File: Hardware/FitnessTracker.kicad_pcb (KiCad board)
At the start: 2 copper layers, 16.6 x 16.7 mm, 8 parts, among them IC1 MAX30102, Q1 BSS138, Q2 BSS138, Q3 BSS138, U1 STM32WB15CCU6E, U2 LIS2DS12TR, U3 MS560702BA03-50, U4 ublox_SAM-M8Q

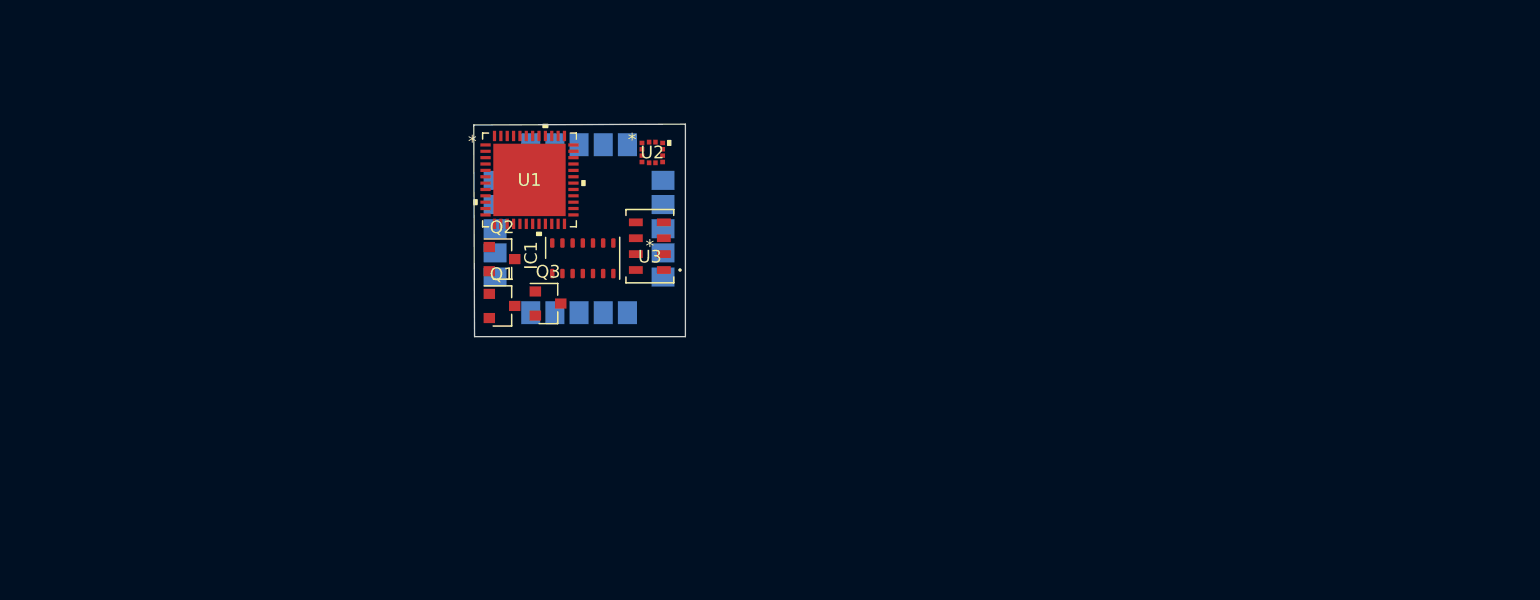
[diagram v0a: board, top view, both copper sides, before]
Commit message: schematic complete, begining pcb layout process
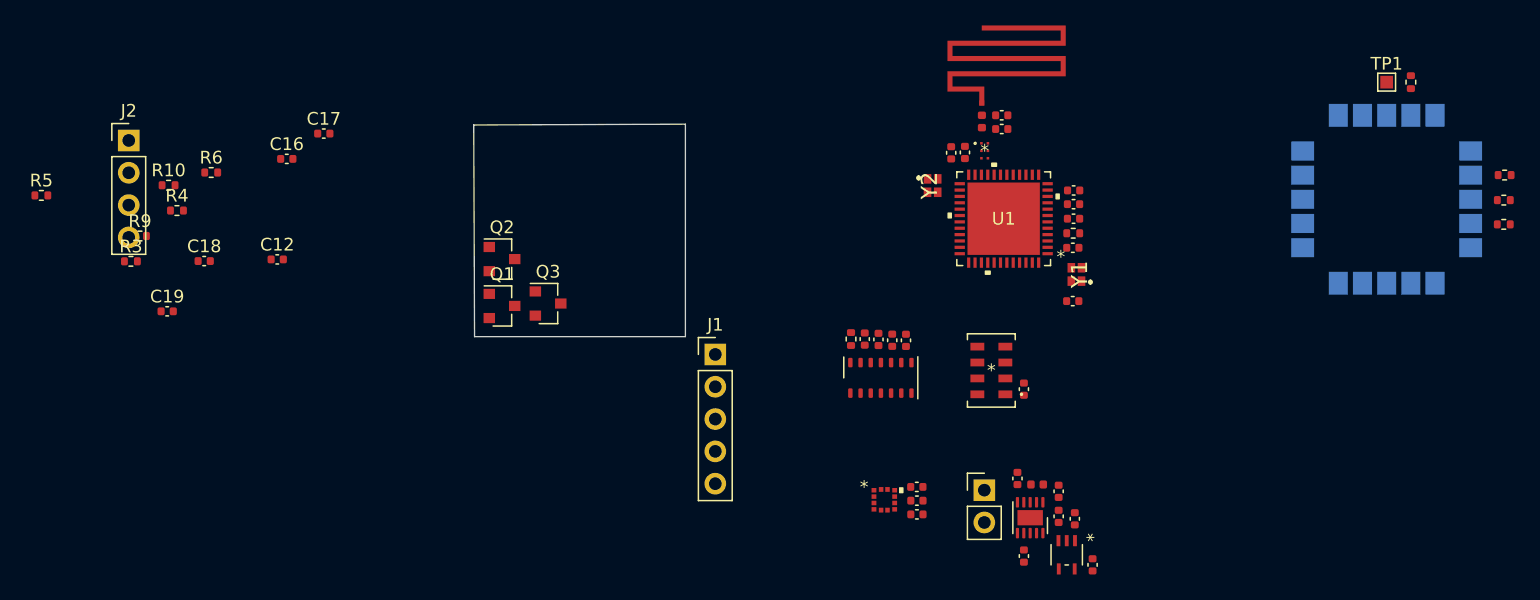
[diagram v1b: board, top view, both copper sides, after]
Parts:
- added AE1: MLPF-WB55-01E3, footprints:MLPF-WB55-01E3, F.Cu at (179.3, 73.9)
- added AE2: Meander Antenna 2.4GHz, footprints:2.4GHz Antenna, F.Cu at (179.3, 70.4)
- added BT1: LiPo, Connector_PinHeader_2.54mm:PinHeader_1x02_P2.54mm_Vertical, F.Cu at (179.3, 100.6)
- added C1: 0.1uF, Capacitor_SMD:C_0402_1005Metric, F.Cu at (169.9, 88.7)
- added C10: 0.1uF, Capacitor_SMD:C_0402_1005Metric, F.Cu at (173.1, 88.8)
- added C11: 100nF, Capacitor_SMD:C_0402_1005Metric, F.Cu at (176.7, 74.1)
- added C12: 4.7uF, Capacitor_SMD:C_0402_1005Metric, F.Cu at (123.7, 82.4)
- added C13: 10uF, Capacitor_SMD:C_0402_1005Metric, F.Cu at (174.0, 101.4)
- added C14: 0.1uF, Capacitor_SMD:C_0402_1005Metric, F.Cu at (174.0, 100.3)
- added C15: 0.1uF, Capacitor_SMD:C_0402_1005Metric, F.Cu at (174.0, 102.5)
- added C16: 100nF, Capacitor_SMD:C_0402_1005Metric, F.Cu at (124.4, 74.5)
- added C17: 100nF, Capacitor_SMD:C_0402_1005Metric, F.Cu at (127.3, 72.6)
- added C18: 100nF, Capacitor_SMD:C_0402_1005Metric, F.Cu at (117.9, 82.6)
- added C19: 100nF, Capacitor_SMD:C_0402_1005Metric, F.Cu at (115.0, 86.5)
- added C2: 10nF, Capacitor_SMD:C_0402_1005Metric, F.Cu at (186.3, 78.1)
- added C20: 1.2pF, Capacitor_SMD:C_0402_1005Metric, F.Cu at (180.6, 72.2)
- added C21: 1.2pF, Capacitor_SMD:C_0402_1005Metric, F.Cu at (180.6, 71.1)
- added C22: 0.1uF, Capacitor_SMD:C_0402_1005Metric, F.Cu at (182.4, 92.6)
- added C23: 10uF, Capacitor_SMD:C_0402_1005Metric, F.Cu at (181.9, 99.7)
- added C24: 0.1uF, Capacitor_SMD:C_0402_1005Metric, F.Cu at (182.4, 105.8)
- added C25: 10uF, Capacitor_SMD:C_0402_1005Metric, F.Cu at (185.1, 102.6)
- added C26: 10uF, Capacitor_SMD:C_0402_1005Metric, F.Cu at (185.1, 100.7)
- added C27: 1uF, Capacitor_SMD:C_0402_1005Metric, F.Cu at (186.4, 102.8)
- added C28: 1uF, Capacitor_SMD:C_0402_1005Metric, F.Cu at (187.8, 106.5)
- added C3: 10pF, Capacitor_SMD:C_0402_1005Metric, F.Cu at (186.2, 85.7)
- added C4: 4.7uF, Capacitor_SMD:C_0402_1005Metric, F.Cu at (170.9, 88.7)
- added C5: 10pF, Capacitor_SMD:C_0402_1005Metric, F.Cu at (186.2, 81.5)
- added C6: 100pF, Capacitor_SMD:C_0402_1005Metric, F.Cu at (177.7, 74.0)
- added C7: 1uF, Capacitor_SMD:C_0402_1005Metric, F.Cu at (186.3, 79.2)
- added C8: 10uF, Capacitor_SMD:C_0402_1005Metric, F.Cu at (172.0, 88.8)
- added C9: 1uF, Capacitor_SMD:C_0402_1005Metric, F.Cu at (186.3, 77.0)
- added J1: ST_Link, Connector_PinHeader_2.54mm:PinHeader_1x05_P2.54mm_Vertical, F.Cu at (158.1, 89.9)
- added J2: SAM_UART, Connector_PinHeader_2.54mm:PinHeader_1x04_P2.54mm_Vertical, F.Cu at (112.0, 73.1)
- added L1: 3.6nH, Inductor_SMD:L_0402_1005Metric, F.Cu at (179.1, 71.6)
- added L2: 1.5uH, Inductor_SMD:L_0402_1005Metric, F.Cu at (183.4, 100.1)
- added R1: 10K, Resistor_SMD:R_0402_1005Metric, F.Cu at (186.2, 80.4)
- added R10: 1M, Resistor_SMD:R_0402_1005Metric, F.Cu at (115.1, 76.6)
- added R11: 470R, Resistor_SMD:R_0402_1005Metric, F.Cu at (220.1, 79.7)
- added R12: 470R, Resistor_SMD:R_0402_1005Metric, F.Cu at (220.1, 77.8)
- added R2: 1M, Resistor_SMD:R_0402_1005Metric, F.Cu at (168.8, 88.7)
- added R3: 1M, Resistor_SMD:R_0402_1005Metric, F.Cu at (112.2, 82.6)
- added R4: 1M, Resistor_SMD:R_0402_1005Metric, F.Cu at (115.8, 78.6)
- added R5: 1M, Resistor_SMD:R_0402_1005Metric, F.Cu at (105.1, 77.4)
- added R6: 1M, Resistor_SMD:R_0402_1005Metric, F.Cu at (118.5, 75.6)
- added R7: 22R, Resistor_SMD:R_0402_1005Metric, F.Cu at (212.8, 68.5)
- added R8: 22R, Resistor_SMD:R_0402_1005Metric, F.Cu at (220.2, 75.8)
- added R9: 1M, Resistor_SMD:R_0402_1005Metric, F.Cu at (112.9, 80.6)
- added TP1: SAFEBOOT, TestPoint:TestPoint_Pad_1.0x1.0mm, F.Cu at (210.9, 68.5)
- added U5: TPS63031DSK, Package_SON:WSON-10-1EP_2.5x2.5mm_P0.5mm_EP1.2x2mm, F.Cu at (182.9, 102.7)
- added U6: STLQ020C18R, footprints:STLQ020C18R, F.Cu at (185.7, 105.7)
- added Y1: 32.768kHz, footprints:8Q20000MAAVT, F.Cu at (186.5, 83.6)
- added Y2: 32MHz, footprints:8Q20000MAAVT, F.Cu at (175.2, 76.6)
- moved U4 63.5 mm to (210.9, 77.7)
- moved U1 37.4 mm to (180.8, 79.2), turned to 180 degrees
- moved U2 32.8 mm to (171.4, 101.3)
- moved U3 28.6 mm to (179.8, 91.2)
- moved IC1 25.2 mm to (171.1, 91.8)
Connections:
- U1 pad 9: Net-(U1-Pad9) -> ADC_IN5
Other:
- copper layers 2 -> 4

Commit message: completed rough layout of pcb
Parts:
- removed C19: 100nF, Capacitor_SMD:C_0402_1005Metric
- removed Q1: BSS138, Package_TO_SOT_SMD:SOT-23
- removed R3, R4: 1M, Resistor_SMD:R_0402_1005Metric
- added J3: STLINK, Connector_PinHeader_1.00mm:PinHeader_1x04_P1.00mm_Vertical, F.Cu at (178.2, 90.8)
- added J4: LPUART, Connector_PinHeader_1.00mm:PinHeader_1x02_P1.00mm_Vertical, F.Cu at (188.6, 74.2)
- added J5: GPIO, Connector_PinHeader_1.00mm:PinHeader_1x03_P1.00mm_Vertical, F.Cu at (174.0, 90.8)
- added JP1: BOOT, Jumper:SolderJumper-2_P1.3mm_Open_Pad1.0x1.5mm, F.Cu at (188.6, 79.2)
- J1: value ST_Link -> PWR_OUT; footprint Connector_PinHeader_2.54mm:PinHeader_1x05_P2.54mm_Vertical -> Connector_PinHeader_1.00mm:PinHeader_1x02_P1.00mm_Vertical
- J2: value SAM_UART -> GPS_UART; footprint Connector_PinHeader_2.54mm:PinHeader_1x04_P2.54mm_Vertical -> Connector_PinHeader_1.00mm:PinHeader_1x02_P1.00mm_Vertical
- Q2, Q3: footprint Package_TO_SOT_SMD:SOT-23 -> Package_TO_SOT_SMD:SOT-323_SC-70; moved to B.Cu
- R10, R5, R6, R9, TP1: moved to B.Cu
- moved J2 78.5 mm to (188.5, 90.7), turned to 270 degrees
- moved R5 63.3 mm to (167.9, 85.6), turned to 180 degrees
- moved C16 61.7 mm to (185.4, 84.1), turned to 270 degrees
- moved C18 57.5 mm to (175.4, 80.0), turned to 180 degrees
- moved R10 55.7 mm to (170.7, 81.0)
- moved R9 54.2 mm to (167.1, 81.0)
- moved R6 53.8 mm to (171.3, 85.6), turned to 180 degrees
- moved C17 53.5 mm to (180.8, 74.0), turned to 90 degrees
- moved C12 51.6 mm to (175.3, 81.3), turned to 180 degrees
- moved R12 34.7 mm to (186.9, 88.2), turned to 270 degrees
- moved R11 32.4 mm to (188.8, 88.2), turned to 90 degrees
- moved R8 31.7 mm to (188.4, 76.9), turned to 180 degrees
- moved R7 29.8 mm to (183.0, 70.0), turned to 0 degrees
- moved U4 29.6 mm to (181.6, 81.7)
- moved C27 29.4 mm to (167.2, 80.6), turned to 0 degrees
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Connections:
- net 30102_INT renamed HRM_INT
- net LIS_INT1 renamed ACC_INT1
- net LIS_INT2 renamed ACC_INT2
- J1 pad 2: SWDIO -> GND
- J2 pad 1: +3V3 -> GPS_RX
- J2 pad 2: SAM_RX -> GPS_TX
- R1 pad 1: GND -> BOOT0
- R1 pad 2: Net-(R1-Pad2) -> GND
- R11 pad 1: SAM_RX -> GPS_RX
- R12 pad 2: SAM_TX -> GPS_TX
- U1 pad 10: Net-(U1-Pad10) -> SPI_SCK
- U1 pad 11: Net-(U1-Pad11) -> LPUART_TX
- U1 pad 12: Net-(U1-Pad12) -> LPUART_RX
- U1 pad 15: Net-(U1-Pad15) -> SPI_MOSI
- U1 pad 16: Net-(U1-Pad16) -> SPI_MISO
- U1 pad 17: Net-(U1-Pad17) -> ACC_CS
- U1 pad 18: Net-(U1-Pad18) -> BAR_CS
- U1 pad 20: SPI_NSS1 -> Net-(U1-Pad20)
- U1 pad 28: Net-(U1-Pad28) -> PB0
- U1 pad 29: Net-(U1-Pad29) -> PB1
- U1 pad 30: Net-(U1-Pad30) -> PB13
- U1 pad 35: SAM_INT_LV -> GPS_INT_LV
- U1 pad 4: Net-(R1-Pad2) -> BOOT0
- U1 pad 43: SPI_SCK -> SWO
- U1 pad 44: SPI_MISO -> Net-(U1-Pad44)
- U1 pad 45: SPI_MOSI -> Net-(U1-Pad45)
- U1 pad 46: SPI_NSS2 -> Net-(U1-Pad46)
- U2 pad 2: SPI_NSS1 -> ACC_CS
- U3 pad 4: SPI_NSS2 -> BAR_CS
- U4 pad 19: SAM_INT -> GPS_INT
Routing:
- added copper zone on In2.Cu, net +1V8
- added copper zone on In1.Cu, net GND
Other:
- board size 16.6 x 16.7 mm -> 24.1 x 22.9 mm
